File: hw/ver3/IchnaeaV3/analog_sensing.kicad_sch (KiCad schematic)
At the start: 46 parts, among them U10 ADS1220xPW, U18 74HC4051PW, U9 74HC4051PW

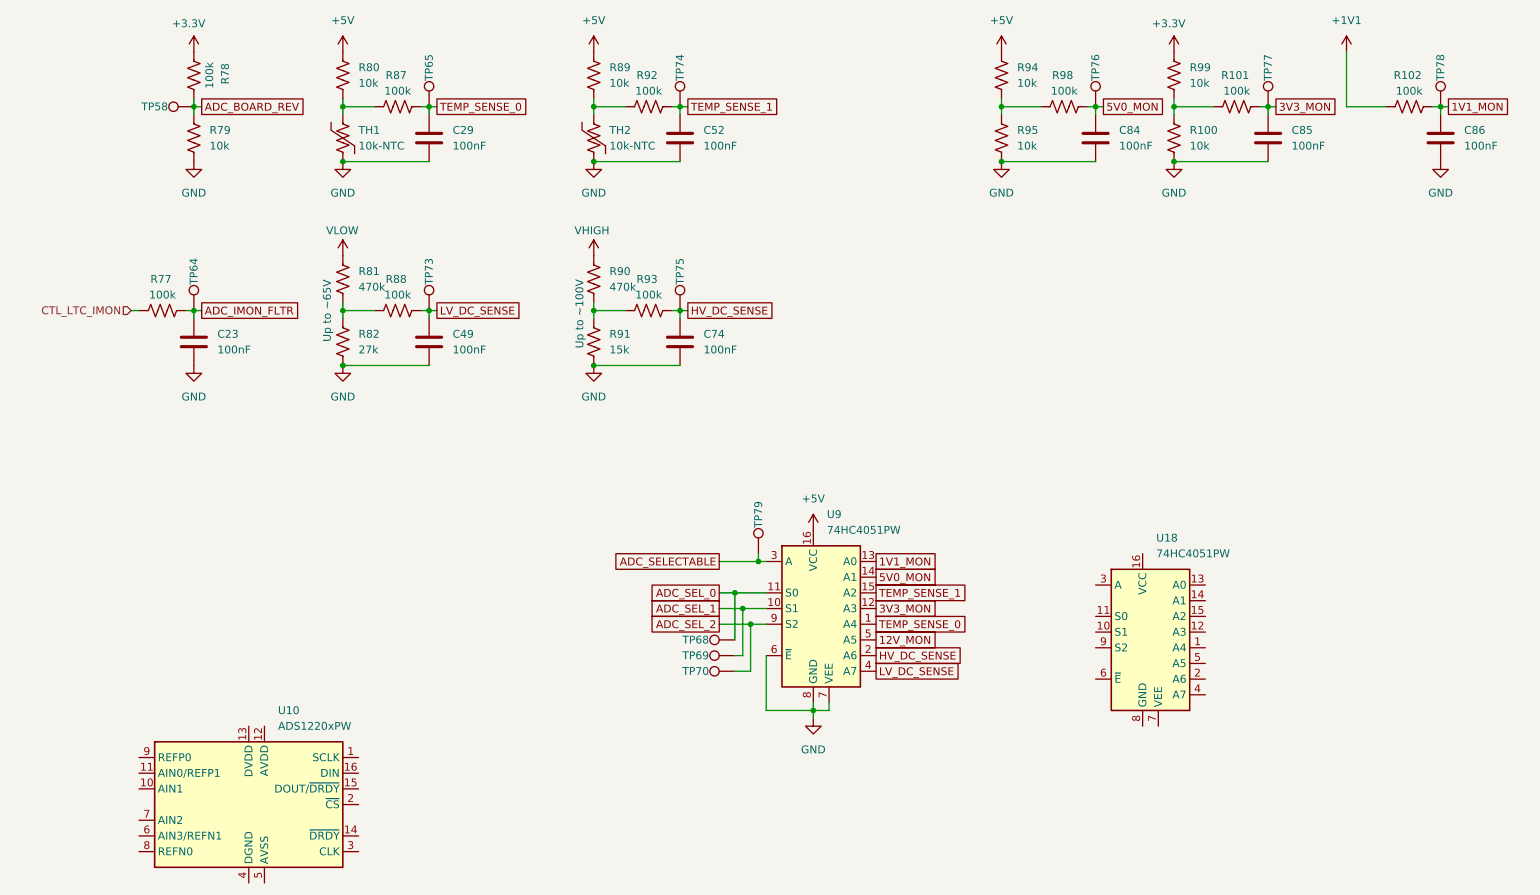
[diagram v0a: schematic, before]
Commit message: Experiment with a new power stage layout
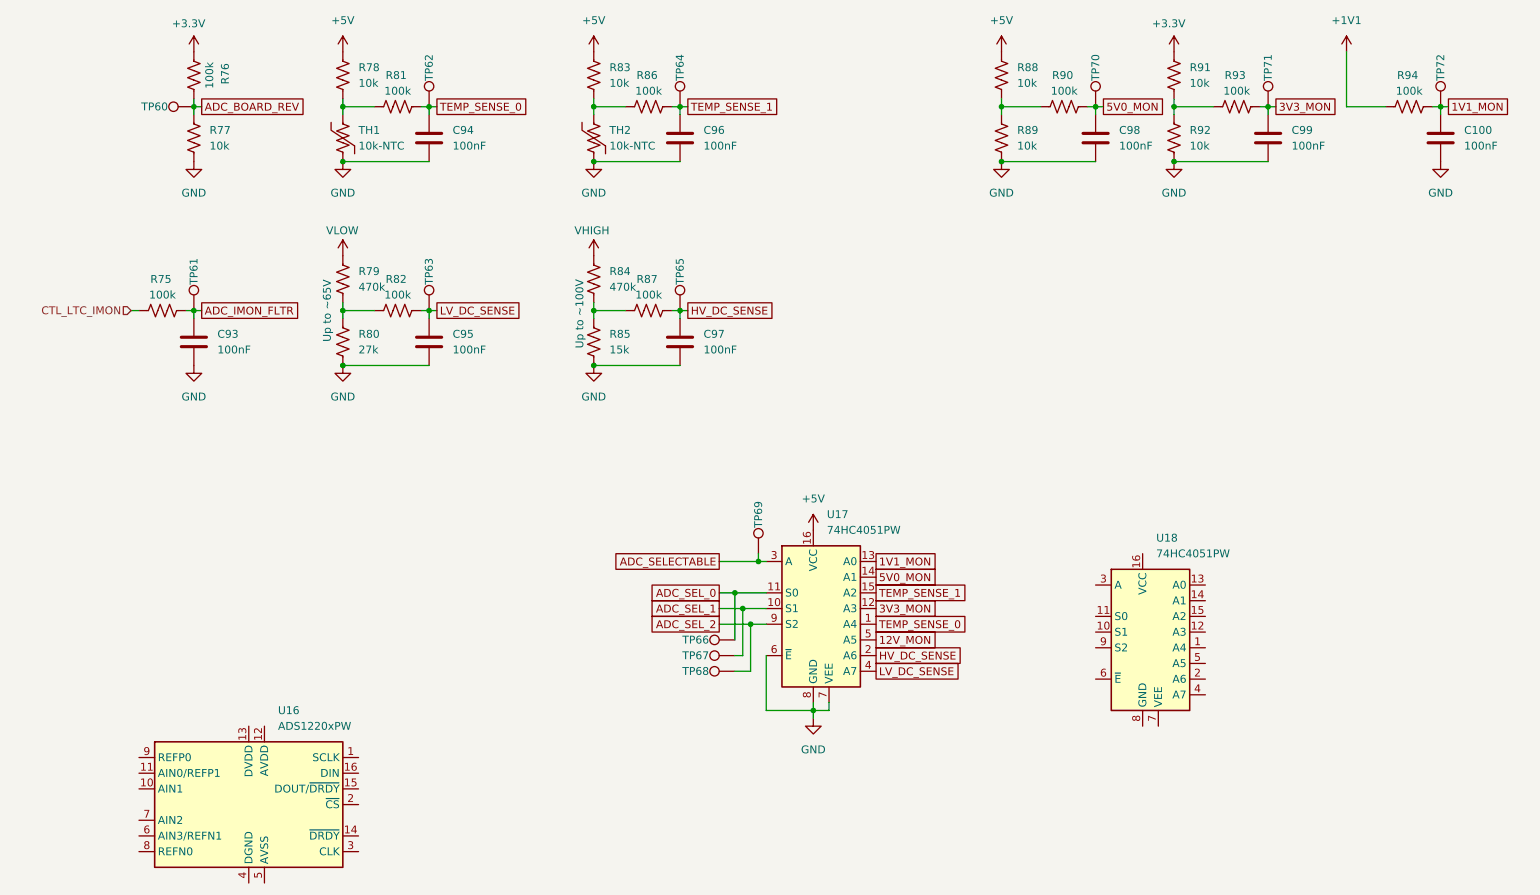
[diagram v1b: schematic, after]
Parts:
- renumbered C86 to C100, C23 to C93, C29 to C94, C49 to C95, C52 to C96, C74 to C97, C84 to C98, C85 to C99, R77 to R75, R78 to R76, R79 to R77, R80 to R78, R81 to R79, R82 to R80, R87 to R81, R88 to R82, R89 to R83, R90 to R84, R91 to R85, R92 to R86, R93 to R87, R94 to R88, R95 to R89, R98 to R90, R99 to R91, R100 to R92, R101 to R93, R102 to R94, TP58 to TP60, TP64 to TP61, TP65 to TP62, TP73 to TP63, TP74 to TP64, TP75 to TP65, TP68 to TP66, TP69 to TP67, TP70 to TP68, TP79 to TP69, TP76 to TP70, TP77 to TP71, TP78 to TP72, U10 to U16, U9 to U17

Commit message: Swiftly correct the design issue.
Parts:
- removed C93: 100nF, Capacitor_SMD:C_0603_1608Metric, symbol Device:C
- removed R75: 100k, Resistor_SMD:R_0603_1608Metric, symbol Device:R_US
- removed TP60, TP61: TestPoint, TestPoint:TestPoint_Pad_D1.0mm, symbol Connector:TestPoint
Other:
- note added: "TODO: Can I delete the 3.3v rail entirely?"
- note added: "TODO: Feed directly into the ADC chip? Except maybe the 5v line"
- note added: "TODO: Need to rev this"

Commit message: Improve more of the power stage layout
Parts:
- removed C100, C99: 100nF, Capacitor_SMD:C_0603_1608Metric, symbol Device:C
- removed R91, R92: 10k, Resistor_SMD:R_0603_1608Metric, symbol Device:R_US
- removed R93, R94: 100k, Resistor_SMD:R_0603_1608Metric, symbol Device:R_US
- removed TP71, TP72: TestPoint, TestPoint:TestPoint_Pad_D1.0mm, symbol Connector:TestPoint
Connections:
- net +3.3V is gone; now on net +5V: R76.1
- net VHIGH renamed VIN
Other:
- note removed: "TODO: Can I delete the 3.3v rail entirely?"
